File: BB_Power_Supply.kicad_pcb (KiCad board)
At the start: 2 copper layers, 41.7 x 53.2 mm, 18 parts, among them J1 Barrel_Jack_Switch, J2 Conn_01x03_Male, J3 Conn_01x02_Male, J4 Screw_Terminal_01x02, J5 Conn_01x03_Male, J6 Conn_01x02_Male, J7 Screw_Terminal_01x02, U1 LM317_TO-220, U2 LM7805_TO220

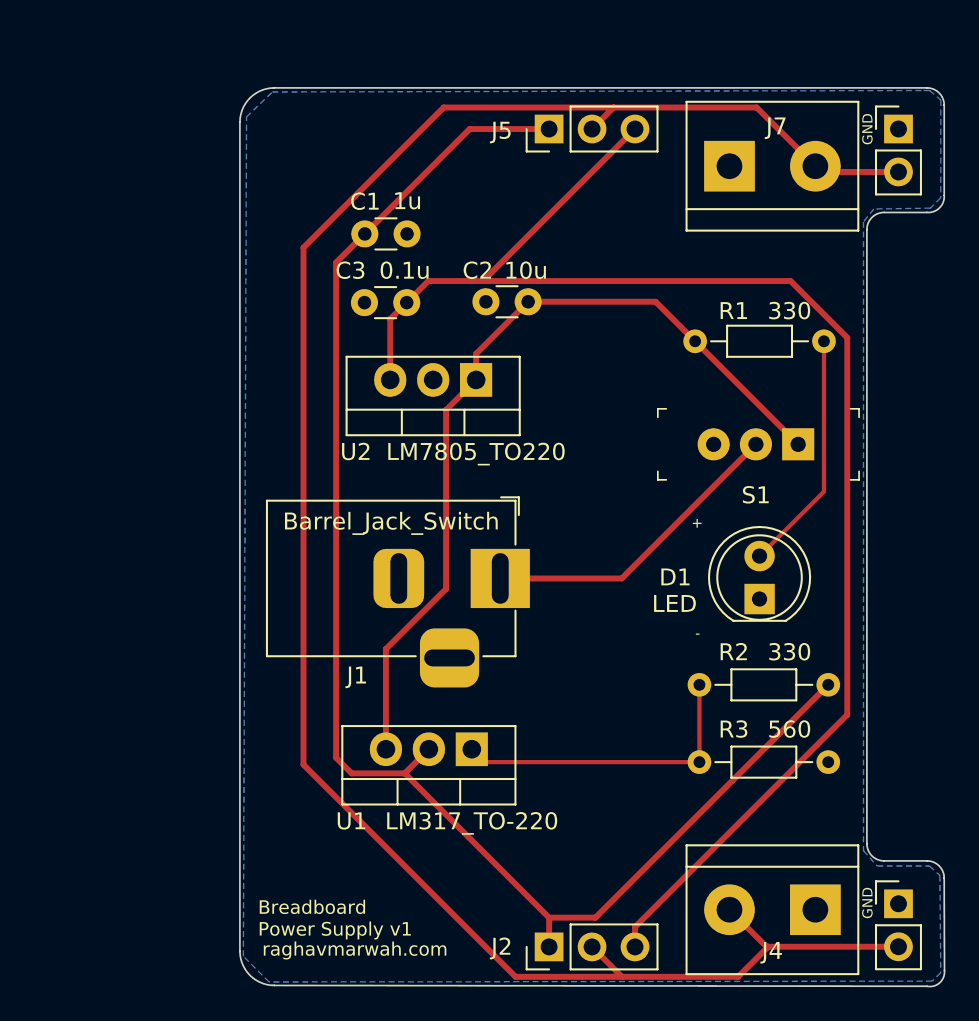
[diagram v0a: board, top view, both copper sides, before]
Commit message: Fix issue with POWER_OUT net
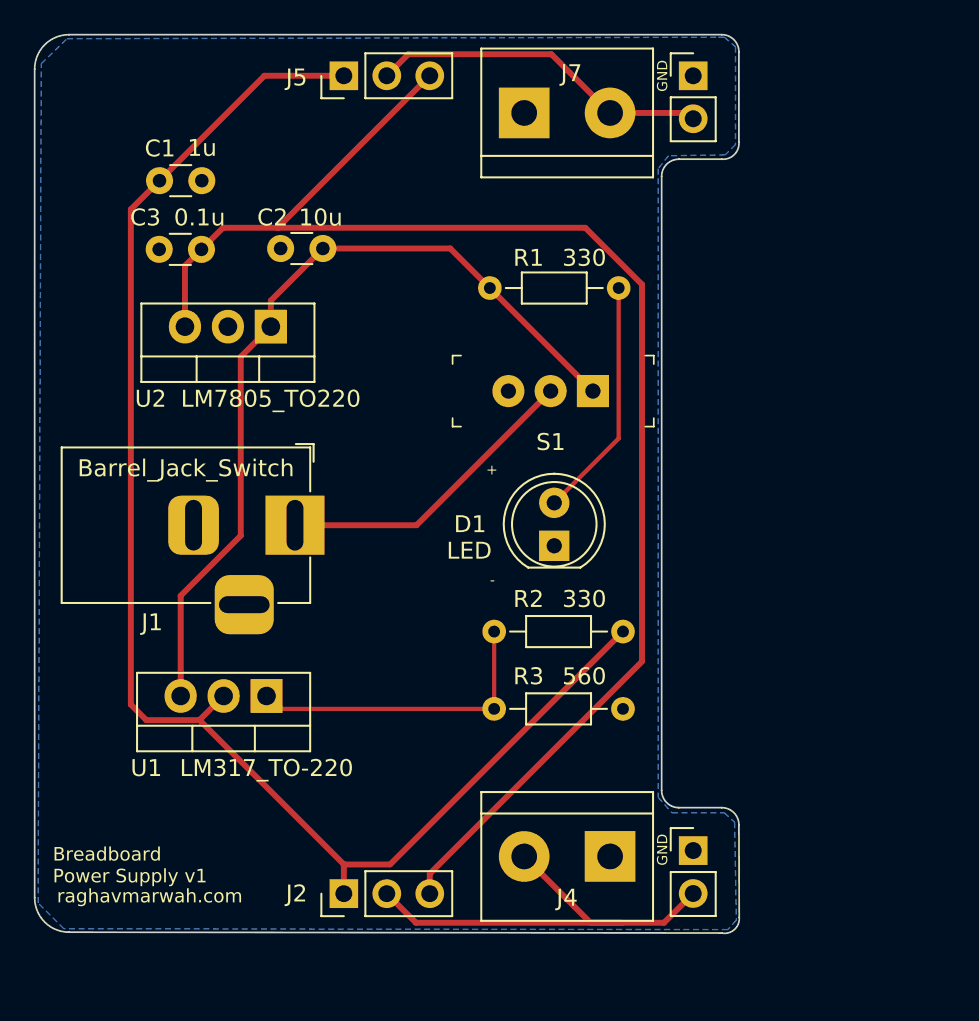
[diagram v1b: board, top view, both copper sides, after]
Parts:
- moved J6 50.5 mm to (159.7, 67.9)
- moved J3 44.4 mm to (159.7, 113.7)
- moved C2 12.5 mm to (137.7, 78.1)
- moved C3 12.5 mm to (130.6, 78.1)
- moved D1 12.5 mm to (151.4, 95.7)
- moved J2 12.5 mm to (139.0, 116.2)
- moved J4 12.5 mm to (154.7, 114.0)
- moved R1 12.5 mm to (155.2, 80.4)
- moved S1 12.5 mm to (153.7, 86.5)
- moved U2 12.5 mm to (134.7, 82.7)
- moved C1 12.5 mm to (128.1, 74.1)
- moved J1 12.5 mm to (136.1, 94.4)
- moved J5 12.5 mm to (139.0, 67.9)
- moved J7 12.5 mm to (149.7, 70.1)
- moved R2 12.5 mm to (147.9, 100.7)
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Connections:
- J2 pad 2: /POWER_OUT -> /POWER_OUT_BOTTOM
- J3 pad 2: /POWER_OUT -> /POWER_OUT_BOTTOM
- J4 pad 2: /POWER_OUT -> /POWER_OUT_BOTTOM
- J5 pad 2: /POWER_OUT -> /POWER_OUT_TOP
- J6 pad 2: /POWER_OUT -> /POWER_OUT_TOP
- J7 pad 2: /POWER_OUT -> /POWER_OUT_TOP
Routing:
- net /POWER_OUT: track 119.4 -> 0.00 mm
- net /POWER_OUT_BOTTOM: track 0.00 -> 27.0 mm
- net /POWER_OUT_TOP: track 0.00 -> 20.2 mm
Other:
- outline, holes or cut-outs redrawn
